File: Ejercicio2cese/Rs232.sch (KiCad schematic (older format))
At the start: 7 parts, among them J1 DB9-F, U1 SP3232ECN

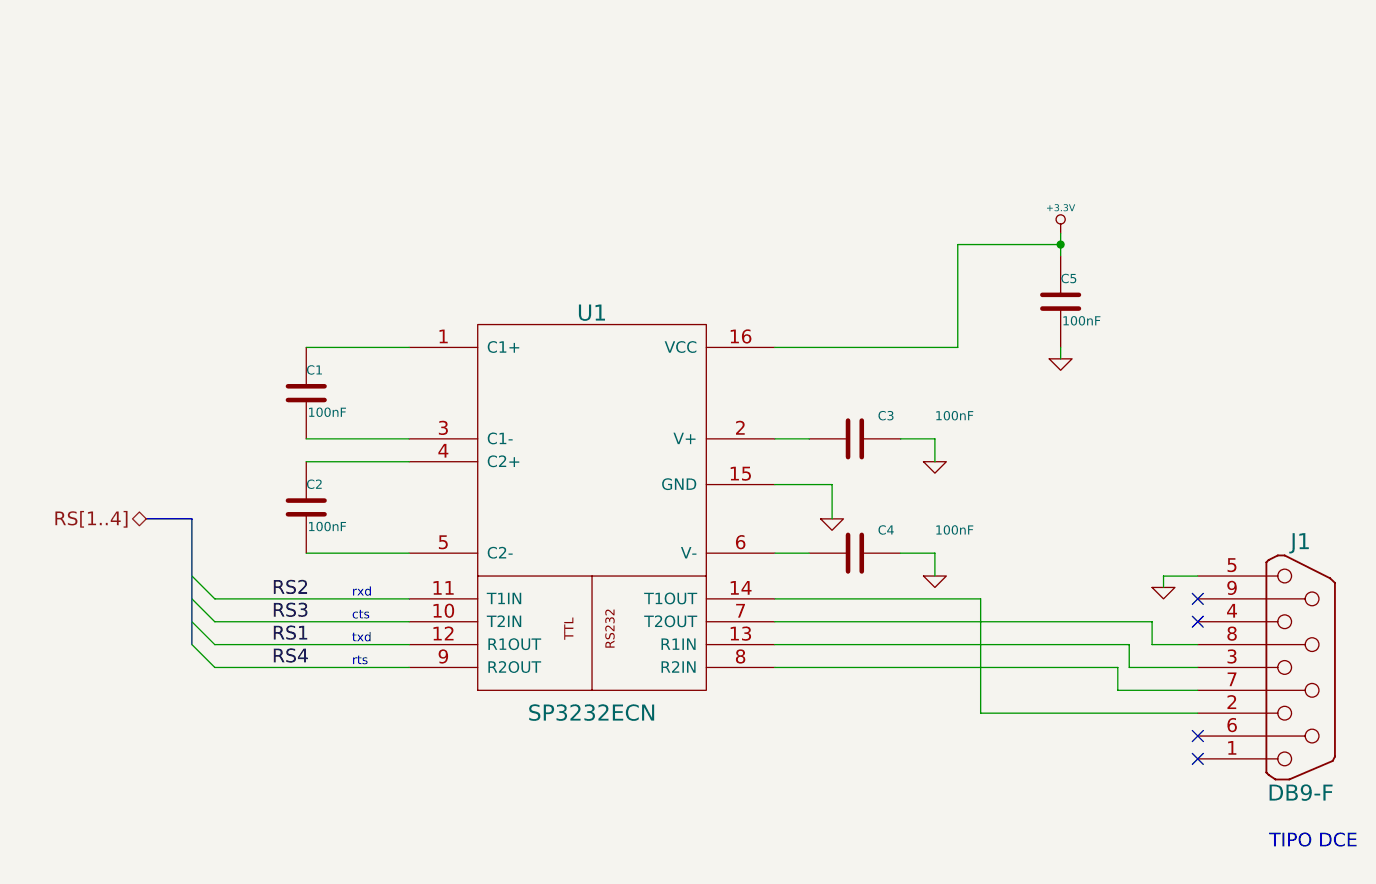
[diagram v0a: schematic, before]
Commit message: Agrego RS232 multipart al esquemático. Cambio nombres de líneas seriales.
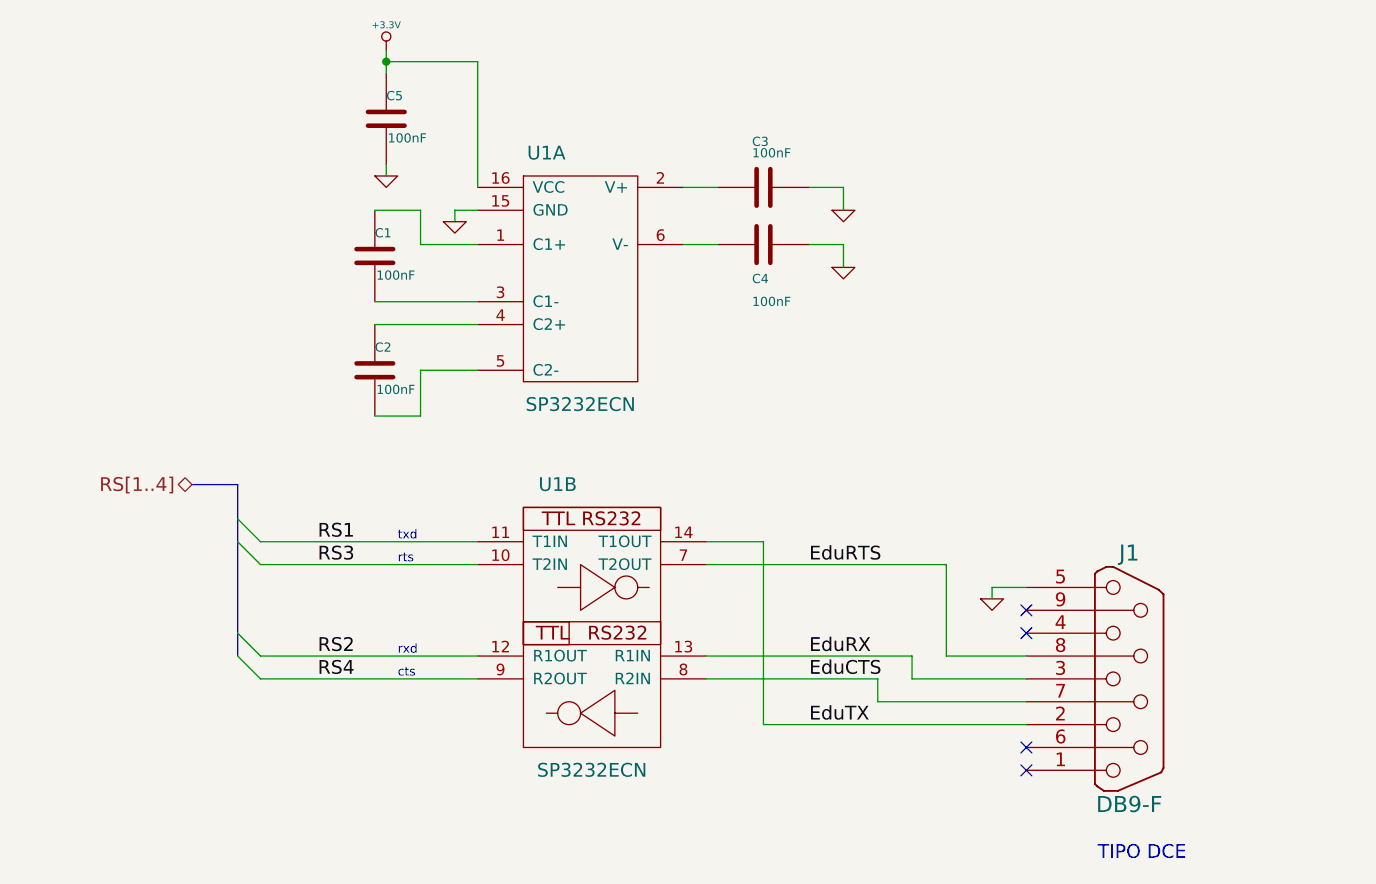
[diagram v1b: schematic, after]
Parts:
- removed U1: SP3232ECN, ej2:SP3232ECN-SOIC16N, symbol SP3232
- added U1: SP3232ECN, symbol MAX232_MP
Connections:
- net +3.3V: now also U1.16 (VCC)
- net GND: now also U1.15 (GND)
- net RS1: now also U1.11 (T1IN)
- net RS2: now also U1.12 (R1OUT)
- net RS3: now also U1.10 (T2IN)
- net RS4: now also U1.9 (R2OUT)
- net EduTX: now reaches J1.2
- net EduTX: now also U1.14 (T1OUT)
- net EduRX: now reaches J1.3
- net EduRX: now also U1.13 (R1IN)
- net EduCTS: now reaches J1.7 (P7)
- net EduCTS: now also U1.8 (R2IN)
- net EduRTS: now reaches J1.8 (P8)
- net EduRTS: now also U1.7 (T2OUT)
- net at C1.1: now also U1.1 (C1+)
- net at C3.2: now also U1.2 (V+)
- net at C1.2: now also U1.3 (C1-)
- net at C2.1: now also U1.4 (C2+)
- net at C2.2: now also U1.5 (C2-)
- net at C4.2: now also U1.6 (V-)
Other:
- moved on the sheet: C1, C2, C3, C4, C5, J1

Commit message: Correcciones en los campos de información para KiCost.
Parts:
- C3: Digikey# (none) -> 311-1179-1-ND; digikey# 311-1179-1-ND -> (none)
- U1: Diegikey# 1016-1803-1-ND -> (none); Digikey# (none) -> 1016-1803-1-ND
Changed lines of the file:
@@
 F 2 "Capacitors_SMD:C_1206_HandSoldering" H 5738 2300 30  0001 C CNN
 F 3 "http://www.yageo.com/documents/recent/UPY-GPHC_X7R_6.3V-to-50V-v12.pdf" H 5700 2450 60  0001 C CNN
-F 4 "311-1179-1-ND" H 5700 2450 60  0001 C CNN "digikey#"
+F 4 "311-1179-1-ND" H 5700 2450 60  0001 C CNN "Digikey#"
 	1    5700 2450
 	0    1    1    0
@@
 F 4 "Exar" H 4950 4350 60  0001 C CNN "Manf"
 F 5 "SP3232ECN-L/TR" H 4950 4350 60  0001 C CNN "Manf#"
-F 6 "1016-1803-1-ND" H 4950 4350 60  0001 C CNN "Diegikey#"
+F 6 "1016-1803-1-ND" H 4950 4350 60  0001 C CNN "Digikey#"
 	2    4950 4350
 	1    0    0    -1

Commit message: Corrección campos del multiparte.
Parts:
- U1: Digikey# (none) -> 1016-1803-1-ND; Manf (none) -> Exar; Manf# (none) -> SP3232ECN-L/TR
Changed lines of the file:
@@
 EESchema Schematic File Version 2
 LIBS:ej2
-LIBS:power
-LIBS:fiducial
-LIBS:max232_mp
 LIBS:ej2-cache
 EELAYER 25 0
@@
 D7 83 7C 1A 00 80 0B F5 7C DA 77 F9 12 00 00 77 D8 F4 F5 E3 3E 81 D3 84 00 BC 9C 1F 9E 53 EF 5E
 56 13 80 F1 D0 10 7F 62 4C 03 40 06 D8 7F 03 40 06 5F ED 80 FF 91 20 12 25 DF 00 00 00 00 49 45
-4E 44 AE 42 60 82 00
+4E 44 AE 42 60 82 01
 EndData
 $EndBitmap
@@
 F 2 "" H 4900 2900 60  0000 C CNN
 F 3 "" H 4900 2900 60  0000 C CNN
+F 4 "Exar" H 4900 2900 60  0001 C CNN "Manf"
+F 5 "SP3232ECN-L/TR" H 4900 2900 60  0001 C CNN "Manf#"
+F 6 "1016-1803-1-ND" H 4900 2900 60  0001 C CNN "Digikey#"
 	1    4900 2900
 	1    0    0    -1

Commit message: Reparo asignación de footprint para U1.
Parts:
- U1: footprint (none) -> ej2:SP3232ECN-SOIC16N
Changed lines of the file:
@@
 D7 83 7C 1A 00 80 0B F5 7C DA 77 F9 12 00 00 77 D8 F4 F5 E3 3E 81 D3 84 00 BC 9C 1F 9E 53 EF 5E
 56 13 80 F1 D0 10 7F 62 4C 03 40 06 D8 7F 03 40 06 5F ED 80 FF 91 20 12 25 DF 00 00 00 00 49 45
-4E 44 AE 42 60 82 01
+4E 44 AE 42 60 82 00
 EndData
 $EndBitmap
@@
 F 0 "U1" H 4750 3500 60  0000 C CNN
 F 1 "SP3232ECN" H 4900 2400 60  0000 C CNN
-F 2 "" H 4900 2900 60  0000 C CNN
+F 2 "ej2:SP3232ECN-SOIC16N" H 4900 2900 60  0001 C CNN
 F 3 "" H 4900 2900 60  0000 C CNN
 F 4 "Exar" H 4900 2900 60  0001 C CNN "Manf"
